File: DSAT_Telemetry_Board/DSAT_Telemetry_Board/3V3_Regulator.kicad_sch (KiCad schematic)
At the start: 5 parts

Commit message: More footprints
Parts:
- C? (x2): footprint (none) -> Capacitor_SMD:C_0201_0603Metric
- R?: footprint (none) -> Resistor_SMD:R_1206_3216Metric
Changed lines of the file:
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@@
       (effects (font (size 1.27 1.27)) (justify right))
     )
-    (property "Footprint" "" (id 2) (at 144.4752 86.36 0)
+    (property "Footprint" "Capacitor_SMD:C_0201_0603Metric" (id 2) (at 144.4752 86.36 0)
       (effects (font (size 1.27 1.27)) hide)
     )
@@
       (effects (font (size 1.27 1.27)) (justify right))
     )
-    (property "Footprint" "" (id 2) (at 168.6052 86.36 0)
+    (property "Footprint" "Capacitor_SMD:C_0201_0603Metric" (id 2) (at 168.6052 86.36 0)
       (effects (font (size 1.27 1.27)) hide)
     )
@@
       (effects (font (size 1.27 1.27)) (justify left))
     )
-    (property "Footprint" "" (id 2) (at 181.102 88.9 90)
+    (property "Footprint" "Resistor_SMD:R_1206_3216Metric" (id 2) (at 181.102 88.9 90)
       (effects (font (size 1.27 1.27)) hide)
     )
-    (property "Datasheet" "~" (id 3) (at 182.88 88.9 0)
+    (property "Datasheet" "https://www.digikey.com/en/products/detail/panasonic-electronic-components/ERA-8ARW102V/5141111" (id 3) (at 182.88 88.9 0)
       (effects (font (size 1.27 1.27)) hide)
     )

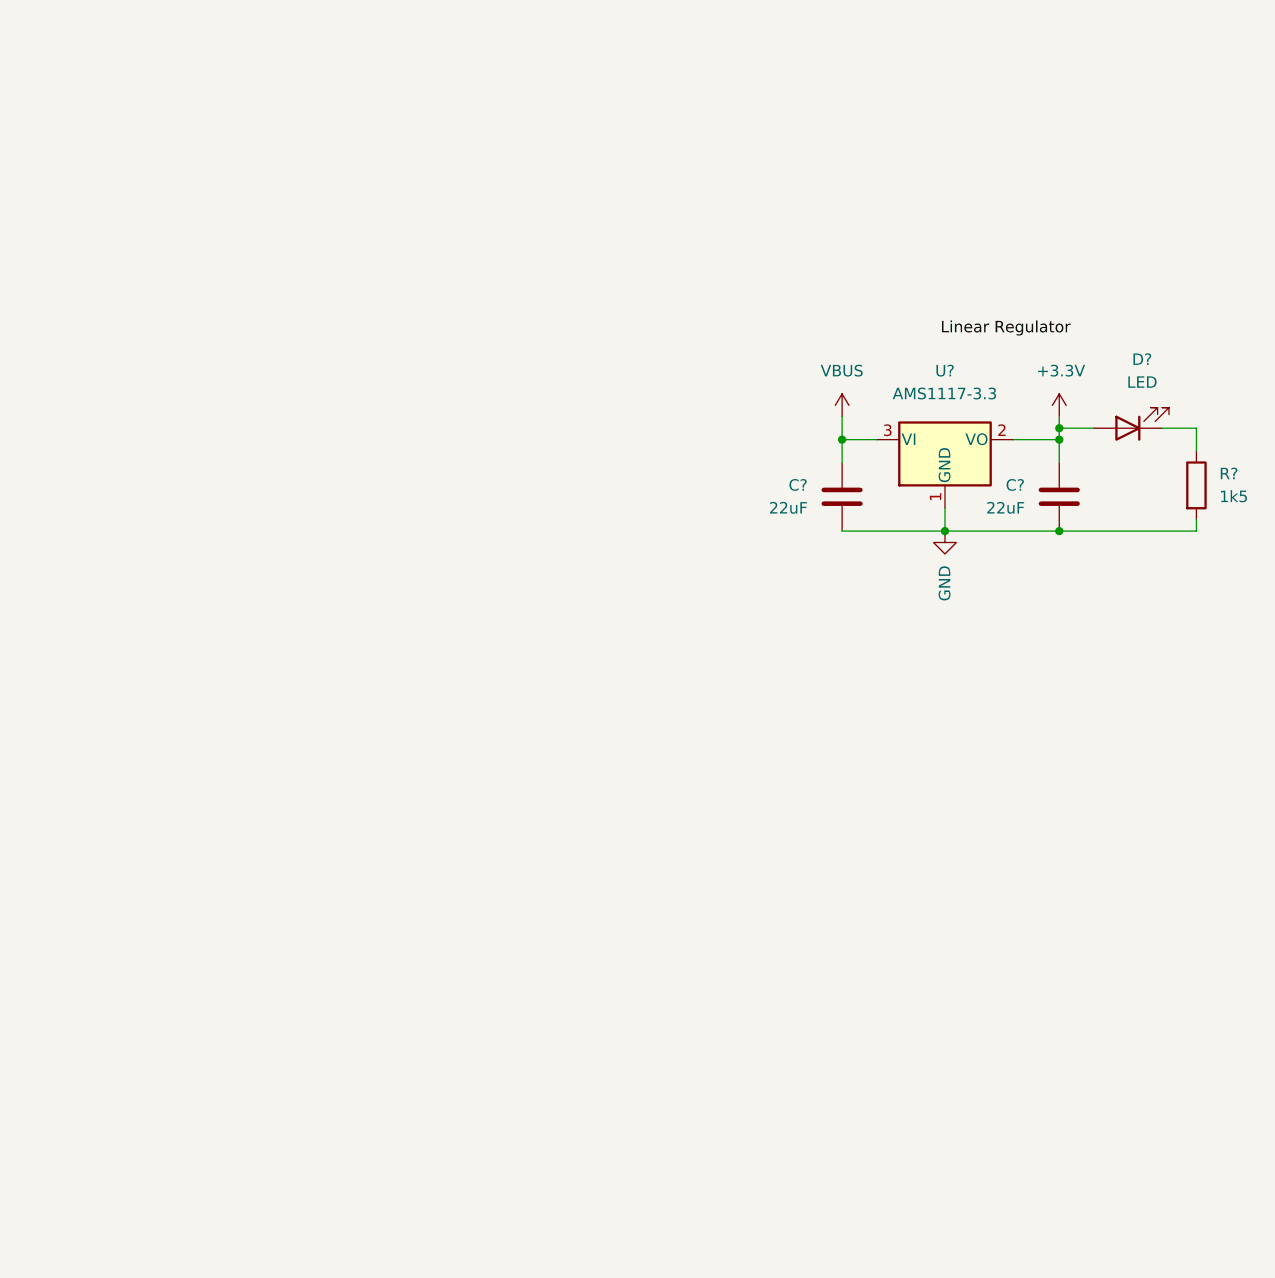
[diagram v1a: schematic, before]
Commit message: RX_SWitch, test points
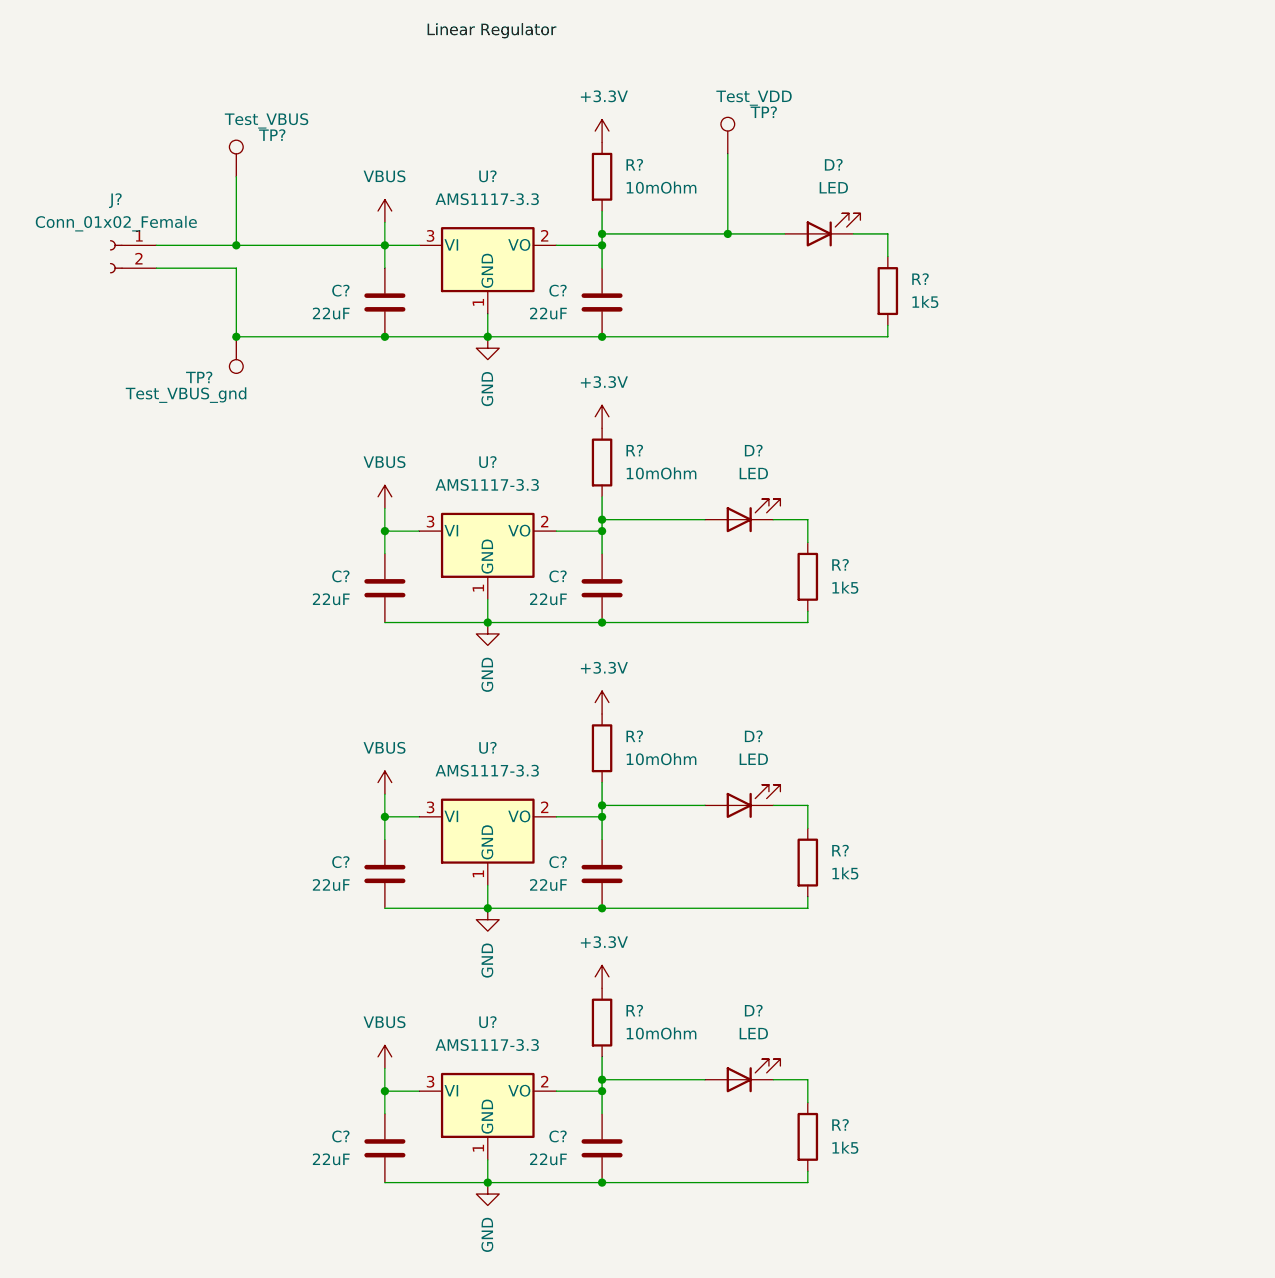
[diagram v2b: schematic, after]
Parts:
- removed C? (x2): 22uF, Capacitor_SMD:C_0201_0603Metric, symbol Device:C
- removed D?: LED, symbol Device:LED
- removed R?: 1k5, Resistor_SMD:R_1206_3216Metric, symbol Device:R
- removed U?: AMS1117-3.3, Package_TO_SOT_SMD:SOT-223-3_TabPin2, symbol Regulator_Linear:AMS1117-3.3
- added C? (x8): 22uF, Capacitor_SMD:C_0402_1005Metric_Pad0.74x0.62mm_HandSolder, symbol Device:C
- added D? (x4): LED, LED_SMD:LED_0402_1005Metric, symbol Device:LED
- added J?: Conn_01x02_Female, Footprints:EDGE_PADS, symbol Connector:Conn_01x02_Female
- added R? (x4): 10mOhm, Resistor_SMD:R_0402_1005Metric_Pad0.72x0.64mm_HandSolder, symbol Device:R
- added R? (x4): 1k5, Resistor_SMD:R_0402_1005Metric_Pad0.72x0.64mm_HandSolder, symbol Device:R
- added TP?: Test_VDD, TestPoint:TestPoint_Pad_D2.5mm, symbol Connector:TestPoint
- added TP?: Test_VBUS, TestPoint:TestPoint_Pad_D2.5mm, symbol Connector:TestPoint
- added TP?: Test_VBUS_gnd, TestPoint:TestPoint_Pad_D2.5mm, symbol Connector:TestPoint
- added U? (x4): AMS1117-3.3, Package_TO_SOT_SMD:SOT-223-3_TabPin2, symbol Regulator_Linear:AMS1117-3.3
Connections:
- net +3.3V: now also R?.1, R?.1, R?.1, R?.1
- net GND: now also C?.1, C?.1, C?.1, C?.1, C?.1, C?.1, C?.1, C?.1, J?.2 (Pin_2), R?.2, R?.2, R?.2, R?.2, TP?.1, U?.1 (GND), U?.1 (GND), U?.1 (GND), U?.1 (GND)
- net VBUS: now also C?.2, C?.2, C?.2, C?.2, J?.1 (Pin_1), TP?.1, U?.3 (VI), U?.3 (VI), U?.3 (VI), U?.3 (VI)
- new net: C?.2, D?.2 (A), R?.2, TP?.1, U?.2 (VO)
- new net: D?.1 (K), R?.1 (x4)
- new net: C?.2, D?.2 (A), R?.2, U?.2 (VO) (x3)

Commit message: RX_SWitch, test points
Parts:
- gave numbers to parts that had none: 28

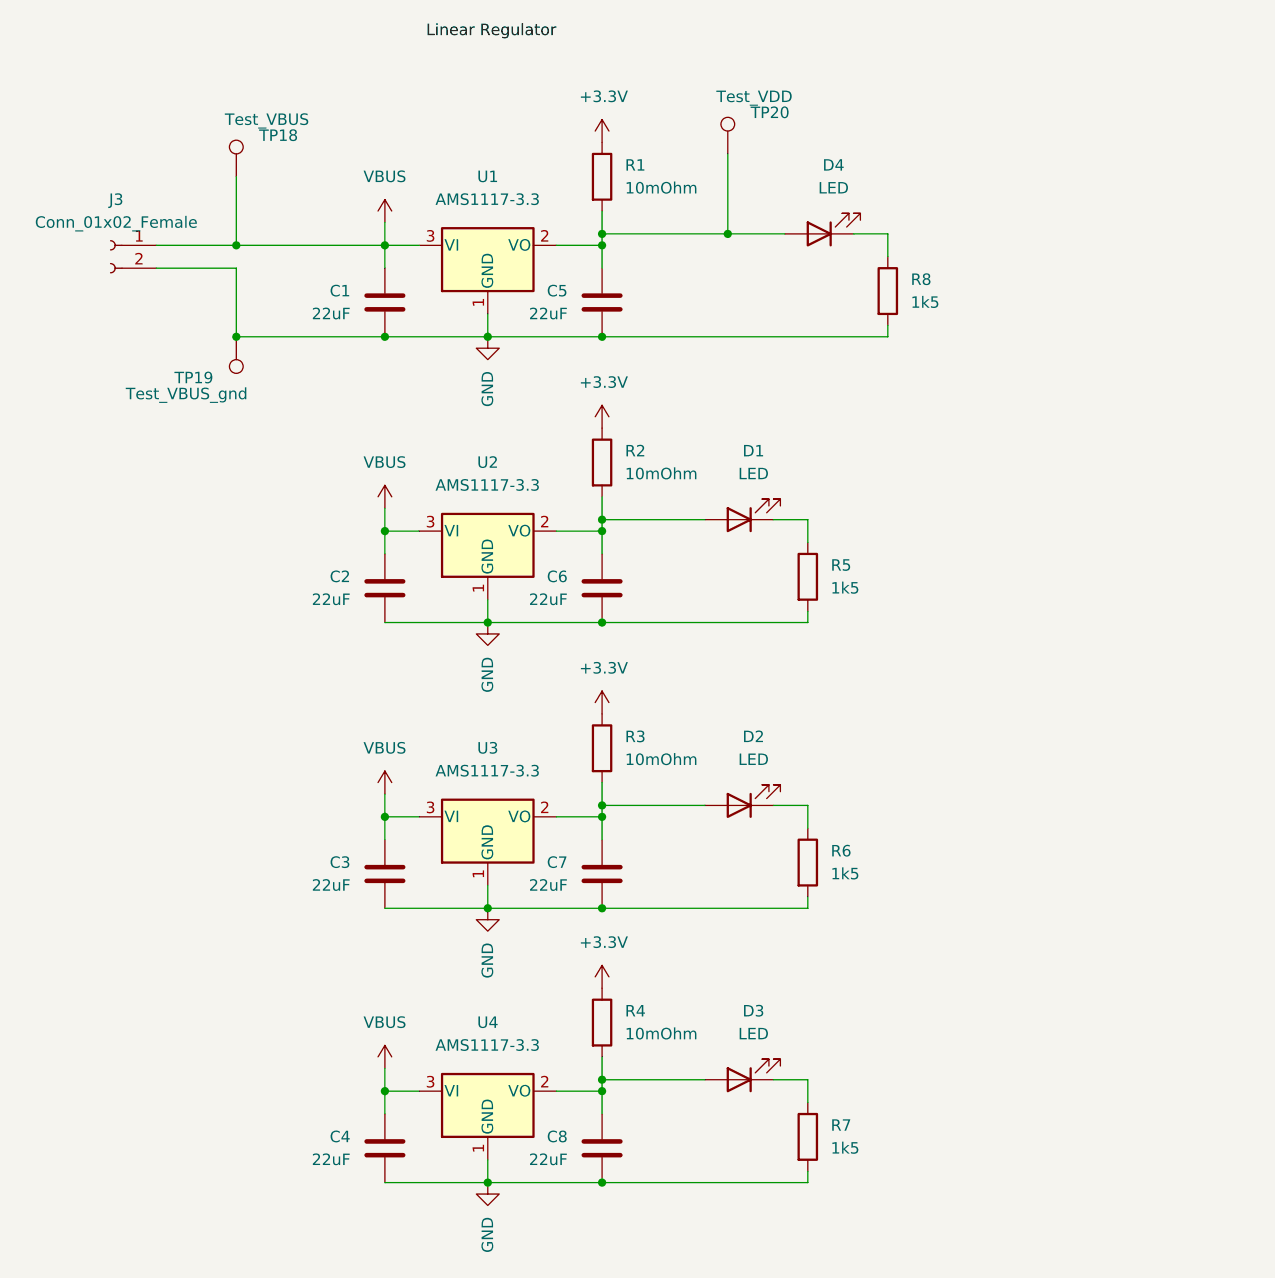
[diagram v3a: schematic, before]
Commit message: Fixed PCB
Added new voltage regulator, reorganized everything, added new lines, fixed most DRC issues. Added ground and power pours. Added more vias.
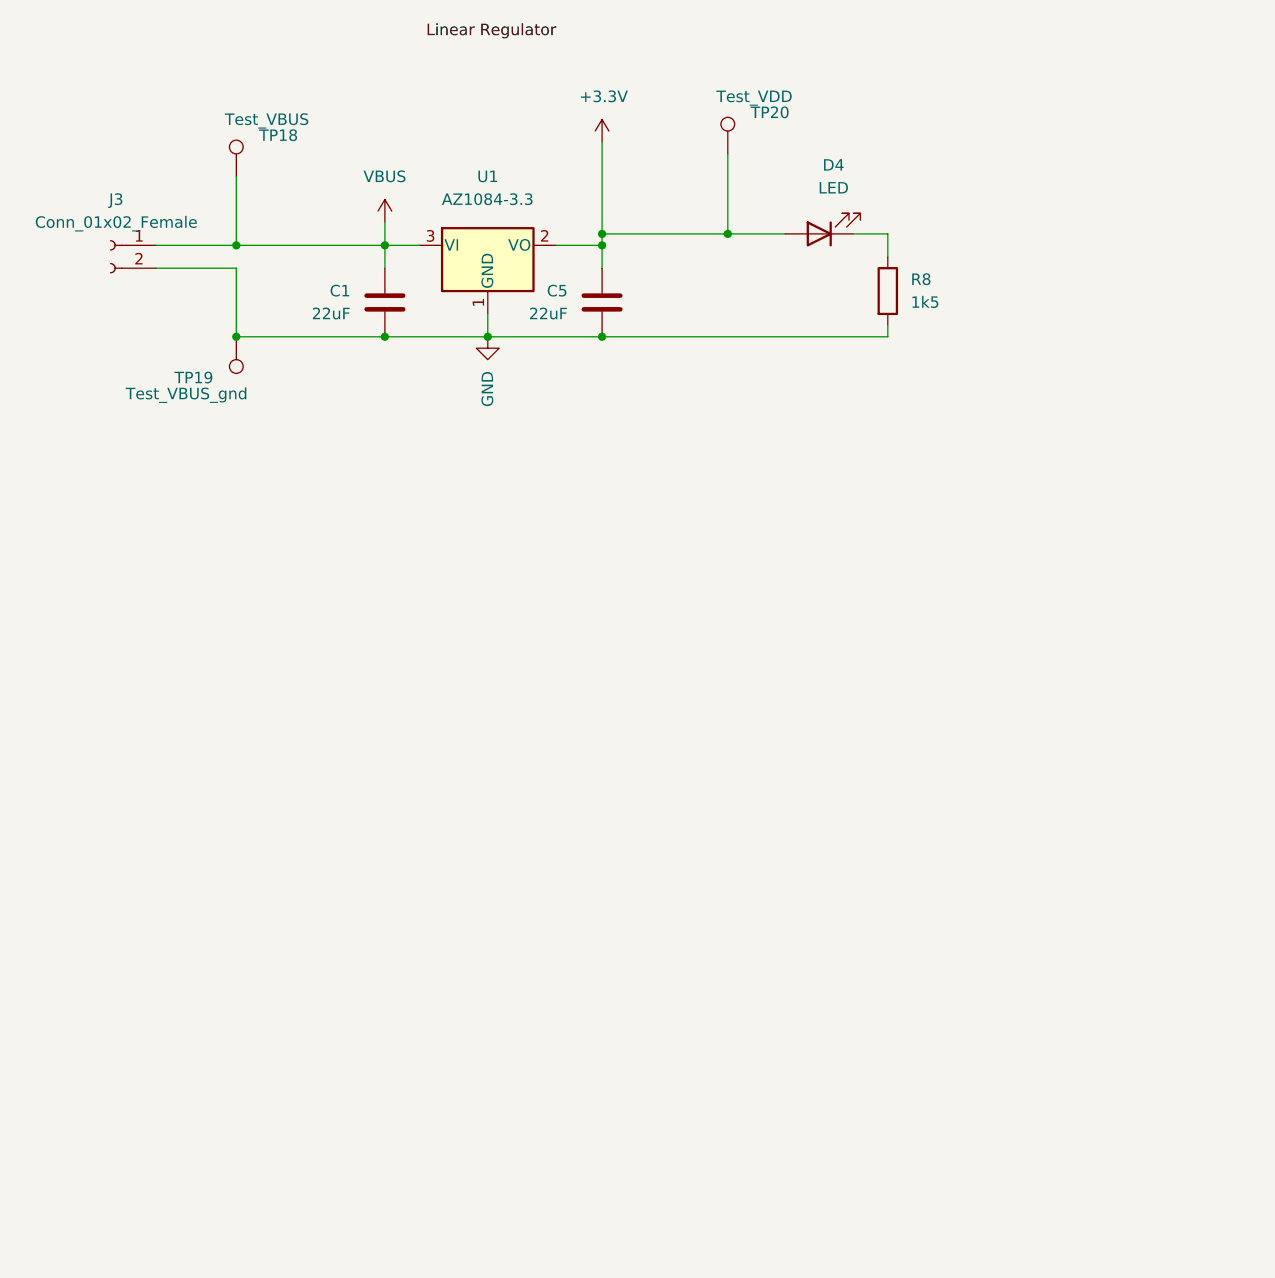
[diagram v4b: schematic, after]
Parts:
- removed C2, C3, C4, C6, C7, C8: 22uF, Capacitor_SMD:C_0402_1005Metric_Pad0.74x0.62mm_HandSolder, symbol Device:C
- removed D1, D2, D3: LED, LED_SMD:LED_0402_1005Metric, symbol Device:LED
- removed R1, R2, R3, R4: 10mOhm, Resistor_SMD:R_0402_1005Metric_Pad0.72x0.64mm_HandSolder, symbol Device:R
- removed R5, R6, R7: 1k5, Resistor_SMD:R_0402_1005Metric_Pad0.72x0.64mm_HandSolder, symbol Device:R
- removed U1, U2, U3, U4: AMS1117-3.3, Package_TO_SOT_SMD:SOT-223-3_TabPin2, symbol Regulator_Linear:AMS1117-3.3
- added U1: AZ1084-3.3, Package_TO_SOT_SMD:TO-252-3_TabPin2, symbol Regulator_Linear:AZ1084-3.3
- J3: footprint Footprints:EDGE_PADS -> TerminalBlock_Phoenix:TerminalBlock_Phoenix_MKDS-1,5-2-5.08_1x02_P5.08mm_Horizontal
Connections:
- net +3.3V: now also C5.2, D4.2 (A), TP20.1, U1.2 (VO)
- net GND: now also U1.1 (GND)
- net VBUS: now also U1.3 (VI)
